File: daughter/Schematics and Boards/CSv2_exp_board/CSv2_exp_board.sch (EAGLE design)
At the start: 144 parts, among them J1 HIROSE-DF40_44-PIN_CONNECTORS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, J2 J-SERIAL-PORT, J3 CORTEX_DEBUG_SMD, J301 HIROSE-DF40_44-PIN_CONNECTORS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, J4 SJ-43514-SMT, J7 J-USB-HIROSE-MICRO-USB, SW1 SPST_TACT-KMR2, SW2 SPST_TACT-KMR2, T1 TPTP10SQ, T10 TPTP10SQ, T11 TPTP10SQ, T2 TPTP10SQ, T3 TPTP10SQ, T4 TPTP10SQ, T5 TPTP10SQ, T6 TPTP10SQ, T7 TPTP10SQ, T8 TPTP10SQ, T9 TPTP10SQ, U1 LOADSWITCH-MIC94164, U10 LOADSWITCH-MIC94164, U11 BMI160, U12 TLV320DAC26IRHB, U13 ADG839YKSZ-500RL7KS_6_ADI-L, U14 LOADSWITCH-MIC94164, U15 LP2980AIM5-2.5/NOPBMF05A_TEX-L, U16 NCP553SQ18T1GSC-82AB_ONS-L, U2 ADA4841-1YRJZ-R7RJ_6-L, U205 MPL3115A2, U3 Value, U4 RFM69HCW, U5 Value, U6 Value, U7 LOADSWITCH-MIC94164, U8 LOADSWITCH-MIC94164, U9 LOADSWITCH-MIC94164, X1 32.768kHz, X2 32.768, X3 uFL, X4 uFL, X5 uFL, X6 uFL

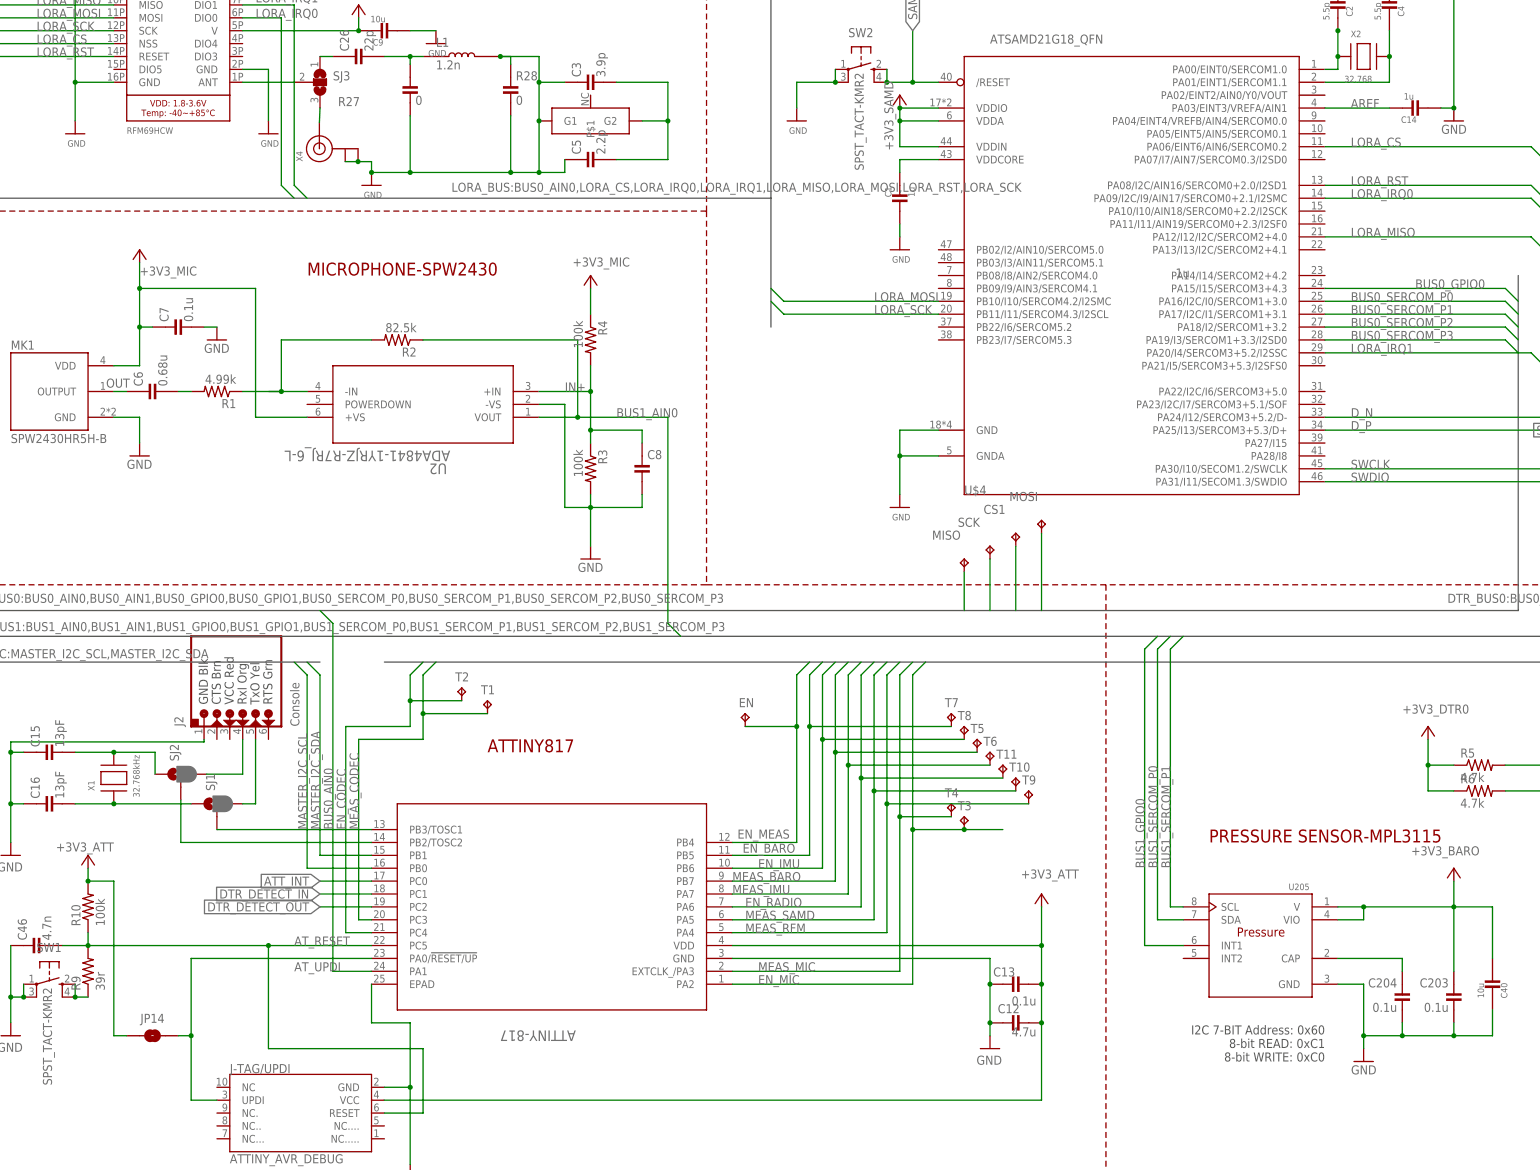
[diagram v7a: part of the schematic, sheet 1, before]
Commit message: DTR-updated BOM
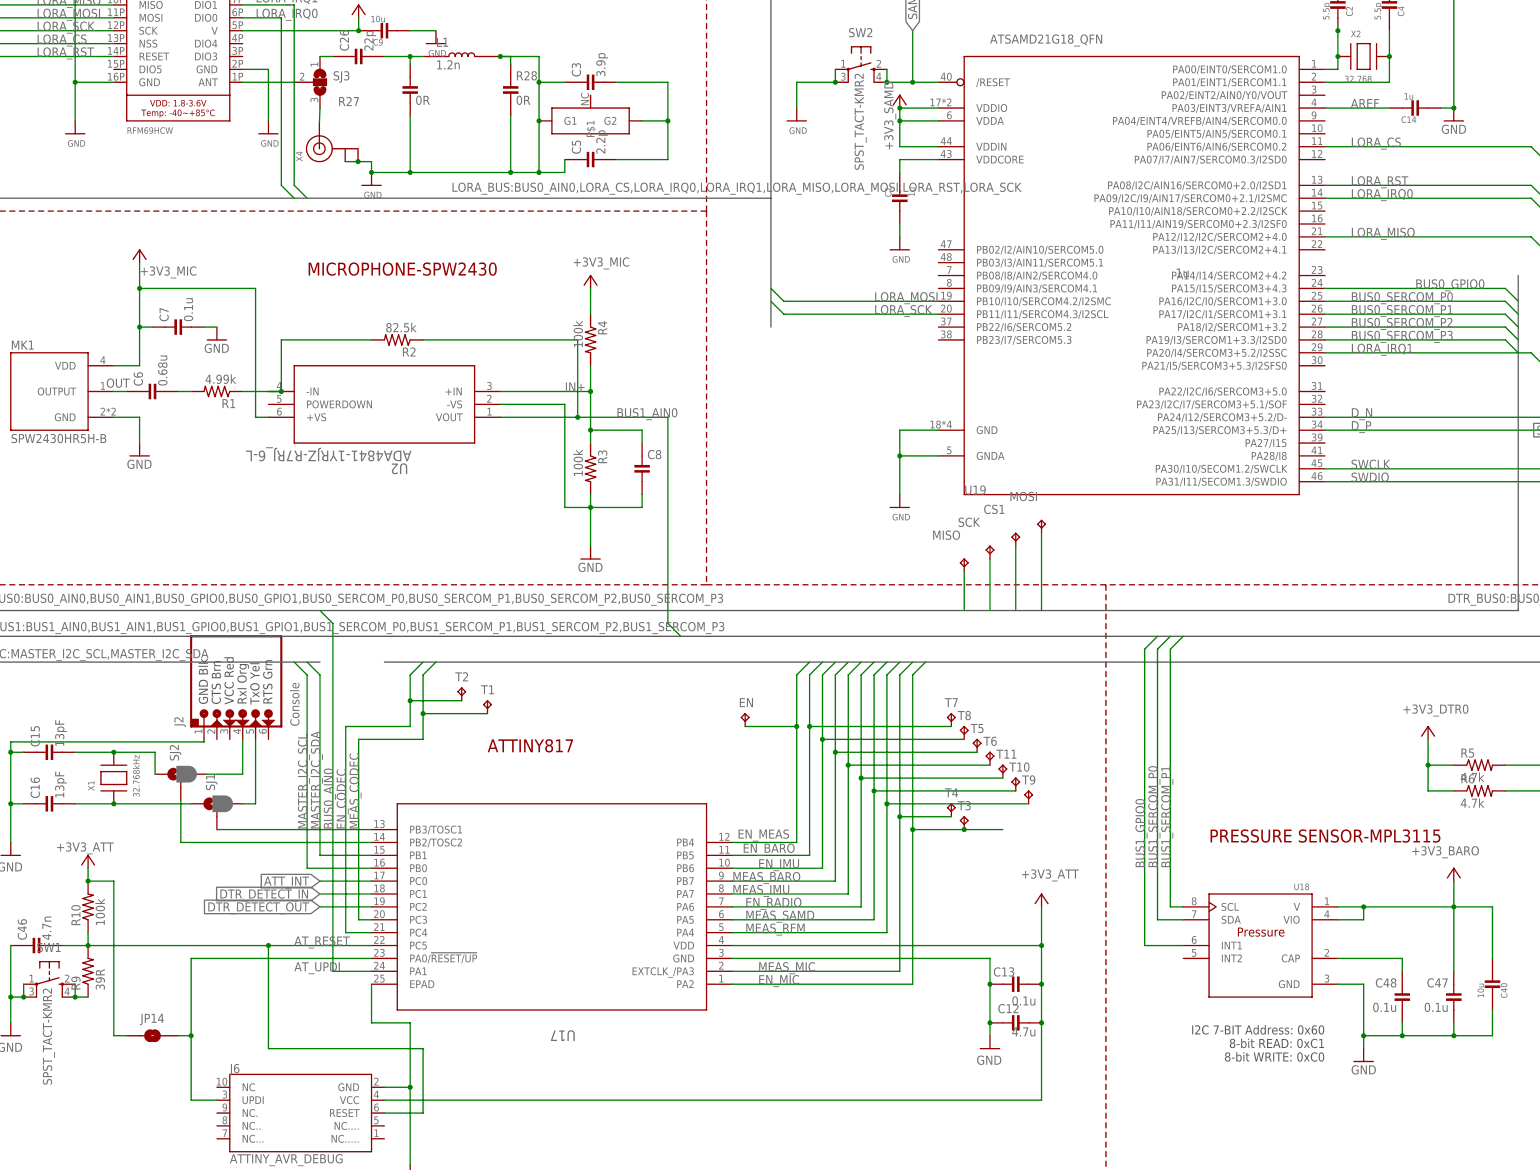
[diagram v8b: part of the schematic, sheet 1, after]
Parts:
- A1: DESC (none) -> RF ANT 915MHZ CHIP SOLDER SMD; MANUFACTURER (none) -> Taoglas; TYPE (none) -> Chip Antenna; Z-HEIGHT (none) -> 0.5mm
- AINT, ASCL, ASDA, CS2, D_IN, D_OUT, JP16, RESET: Z-HEIGHT (none) -> d
- C1, C14: DESC (none) -> CAP CER 1UF 10V X5R 0402; SIZE (none) -> 0402; TYPE (none) -> Capacitor; VOLT (none) -> 10V; Z-HEIGHT (none) -> 0.55mm
- C10, C17, C19, C21, C23, C29: DESC (none) -> CAP CER 1UF 6.3V X5R 0402; HEIGHT (none) -> 0.55mm; SIZE (none) -> 0402; TYPE (none) -> Capacitor; VOLT (none) -> 6.3V
- C11, C18, C20, C22, C30, C43, C44, C45: DESC (none) -> CAP CER 0.1UF 10V X7R 0402; DESCRIPTION (none) -> 0.1µF ±10% 10V Ceramic Capacitor X7R 0402 (1005 Metric); HEIGHT (none) -> 0.55mm; MPN CC0402KRX5R5BB104 -> CC0402KRX7R6BB104; PARTNO CC0402KRX5R5BB104 -> CC0402KRX7R6BB104; SIZE (none) -> 0402; TC X5R -> (none); TYPE (none) -> Capacitor; VOLT (none) -> 10V
- C12: DESC (none) -> CAP CER 4.7UF 10V X5R 0603; HEIGHT (none) -> 0.9mm; SIZE (none) -> 0603; TYPE (none) -> Capacitor; VOLT (none) -> 10V
- C13, C25, C36, C47, C48, C7: DESC (none) -> CAP CER 0.1UF 16V X7R 0402; HEIGHT (none) -> 0.55mm; SIZE (none) -> 0402; TYPE (none) -> Capacitor; VOLT (none) -> 16V
- C15, C16, CS1: TYPE (none) -> Capacitor
- C2: DESC (none) -> CAP CER RF 5.5PF 50V +/-0.1 PF C; SIZE (none) -> 0402; TOL 0.1p -> 0.1pF; TYPE (none) -> Capacitor; VOLT (none) -> 50V; Z-HEIGHT (none) -> 0.55mm
- C24: DESC (none) -> CAP CER 0.1UF 10V X7R 0402; HEIGHT (none) -> 0.55mm; MPN CC0402KRX5R5BB104 -> CC0402KRX7R6BB104; PARTNO CC0402KRX5R5BB104 -> CC0402KRX7R6BB104; SIZE (none) -> 0402; TC X5R -> (none); TYPE (none) -> Capacitor; VOLT (none) -> 10V
- C26: DESC (none) -> CAP CER 22PF 50V C0G/NP0 0402; HEIGHT (none) -> 0.55mm; SIZE (none) -> 0402; TYPE (none) -> Capacitor; VOLT (none) -> 50V
- C3: DESC (none) -> CAP CER 3.9PF 50V C0G/NP0 0402; SIZE (none) -> 0402; TC (none) -> C0G, NP0; TOL 0.05p -> 0.05pF; TYPE (none) -> Capacitor; VOLT (none) -> 50V; Z-HEIGHT (none) -> 0.55mm
- C31, C32: device Capacitors:C-0603 -> Capacitors:C-0805; DESC (none) -> CAP CER 47UF 6.3V X5R 0805; HEIGHT (none) -> 0.95mm; MANUFACTURER AVX -> Murata; MPN 06036D476MAT2A -> GRM219R60J476ME44D; PARTNO 06036D476MAT2A -> GRM219R60J476ME44D; SIZE (none) -> 0805; TYPE (none) -> Capacitor; VOLT (none) -> 6.3V
- C33, C34, C38: DESC (none) -> CAP CER 0.1UF 25V X7R 0402; HEIGHT (none) -> 0.55mm; SIZE (none) -> 0402; TYPE (none) -> Capacitor; VOLT (none) -> 25V
- C35, C39, C40, C9: DESC (none) -> CAP CER 10UF 6.3V X5R 0603; HEIGHT (none) -> 0.9mm; SIZE (none) -> 0603; TYPE (none) -> Capacitor; VOLT (none) -> 6.3V
- C37: DESC (none) -> CAP TANT 10UF 10% 10V 0603; HEIGHT (none) -> 1mm; SIZE (none) -> 0603; TYPE (none) -> Tantalum Capacitor; VOLT (none) -> 10V
- C4: DESC (none) -> CAP CER RF 5.5PF 50V +/-0.1 PF C; SIZE (none) -> 0402; TC C0G,NP0 -> C0G, NP0; TOL 0.1p -> 0.1pF; TYPE (none) -> Capacitor; VOLT (none) -> 50V; Z-HEIGHT (none) -> 0.55mm
- C41: DESC (none) -> CAP TANT 2.2UF 20% 6.3V 0402; HEIGHT (none) -> 0.7mm; MPN (none) -> TACK225M006QTA; SIZE (none) -> 0402; TYPE (none) -> Tantalum Capacitor; VOLT (none) -> 6.3V
- C42: DESC (none) -> CAP CER 1UF 10V X7S 0402; HEIGHT (none) -> 0.55mm; SIZE (none) -> 0402; TYPE (none) -> Capacitor; VOLT (none) -> 10V
- C46: DESC (none) -> CAP CER 4700PF 25V X7R 0402; HEIGHT (none) -> 0.55mm; SIZE (none) -> 0402; TYPE (none) -> Capacitor; VOLT (none) -> 25
- C5: DESC (none) -> CAP CER 2.2PF 50V C0G/NP0 0402; HEIGHT (none) -> 0.55mm; SIZE (none) -> 0402; TC (none) -> C0G, NP0; TOL 0.05p -> 0.05pF; TYPE (none) -> Capacitor; VOLT (none) -> 50V
- C6: DESC (none) -> CAP CER 0.68UF 6.3V X5R 0402; HEIGHT (none) -> 0.55mm; SIZE (none) -> 0402; TYPE (none) -> Capacitor; VOLT (none) -> 6.3V
- C8: DESC (none) -> CAP CER 1UF 10V X5R 0402; SIZE (none) -> 0402; TOL (none) -> 20%; TYPE (none) -> Capacitor; VOLT (none) -> 10V; Z-HEIGHT (none) -> 0.55mm
- J1: DESC (none) -> CONN RCPT 44POS SMD GOLD; HEIGHT (none) -> 3mm; MANUFACTURER (none) -> Hirose; TYPE (none) -> Receptor
- J2: DESC (none) -> CONN HEADER VERT 6POS 2.54MM; TYPE (none) -> Header
- J3, J6: DESC (none) -> CONN HEADER SMD 10POS 1.27MM; MANUFACTURER (none) -> Samtec; TYPE (none) -> Header
- J4: DESC (none) -> CONN JACK 4COND 3.5MM SMD R/A; HEIGHT (none) -> 5mm; MANUFACTURER (none) -> CUI Devices; TYPE (none) -> Audio Jack
- J5: DESC (none) -> CONN PLUG 44POS SMD GOLD; MANUFACTURER (none) -> Hirose; TYPE (none) -> Header
- J7: DESC (none) -> CONN RCPT USB2.0 MICRO AB SMD RA; TYPE (none) -> Receptor
- L1: DESC (none) -> FIXED IND 1.2NH 390MA 100 MOHM; HEIGHT (none) -> 0.45mm; MANUFACTURER (none) -> Murata; SIZE (none) -> 0402; TOL (none) -> 0.05nH; TYPE (none) -> Inductor
- MK1: DESC (none) -> MAMET MIC ANALOG TOP PORT; HEIGHT (none) -> 1.1mm; MANUFACTURER (none) -> Knowles; SIZE (none) -> 0.122" L x 0.098" W (3.10mm x 2.50mm); TYPE (none) -> MEMS Microphone; VOLT (none) -> 1.5V ~ 3.6V
- R1: DESC (none) -> RES SMD 4.99KOHM 0.1% 1/16W 0402; HEIGHT (none) -> 0.4mm; SIZE (none) -> 0402; TC (none) -> ±25ppm/°C; TYPE (none) -> Resistor
- R10, R11: DESC (none) -> RES SMD 100K OHM 1% 1/10W 0402; HEIGHT (none) -> 0.4mm; SIZE (none) -> 0402; TC (none) -> ±100ppm/°C; TYPE (none) -> Resistor
- R12: value (none) -> 0R; DESC (none) -> RES SMD 0 OHM JUMPER 1/2W 1210; HEIGHT (none) -> 0.7mm; MPN (none) -> ERJ-14Y0R00U; SIZE (none) -> 1210; TYPE (none) -> Resistor
- R2: DESC (none) -> RES SMD 82.5KOHM 0.1% 1/16W 0402; HEIGHT (none) -> 0.4mm; SIZE (none) -> 0402; TC (none) -> ±25ppm/°C; TYPE (none) -> Resistor
- R27, R28: value 0 -> 0R; DESC (none) -> RES 0 OHM JUMPER 1/16W 0402; SIZE (none) -> 0402; TYPE (none) -> Resistor
- R3, R4: DESC (none) -> RES SMD 100K OHM 0.1% 1/16W 0402; HEIGHT (none) -> 0.35mm; SIZE (none) -> 0402; TC (none) -> ±25ppm/°C; TYPE (none) -> Resistor
- R5, R6: DESC (none) -> RES SMD 4.7K OHM 1% 1/10W 0402; HEIGHT (none) -> 0.4mm; SIZE (none) -> 0402; TC (none) -> ±100ppm/°C; TYPE (none) -> Resistor
- R7: value 50 -> 50R; device Resistors:R-0805 -> Resistors:R-0402; DESC (none) -> RES SMD 50 OHM 0.1% 1/20W 0402; HEIGHT (none) -> 0.84mm; MPN (none) -> FC0402E50R0BST1; PARTNO Y402250R0000A9R -> FC0402E50R0BST1; SIZE (none) -> 0402; TC (none) -> ±25ppm/°C; TOL 0.05% -> 0.1%; TYPE (none) -> Resistor
- R8: DESC (none) -> RES SMD 2.2K OHM 5% 1/10W 0603; HEIGHT (none) -> 0.55mm; SIZE (none) -> 0603; TC (none) -> ±200ppm/°C; TYPE (none) -> Resistor
- R9: value 39r -> 39R; DESC (none) -> RES SMD 39 OHM 1% 1/10W 0402; HEIGHT (none) -> 0.4mm; SIZE (none) -> 0402; TC (none) -> ±100ppm/°C; TYPE (none) -> Resistor
- R_SENSE: value 1.33 -> 1.33R; DESC (none) -> RES SMD 1.33 OHM 1% 1/16W 0402; HEIGHT (none) -> 0.4mm; SIZE (none) -> 0402; TC (none) -> ±100ppm/°C; TYPE (none) -> Resistor
- SW1, SW2: DESC (none) -> SWITCH TACTILE SPST-NO 0.05A 32V; HEIGHT (none) -> 1.9mm; MANUFACTURER (none) -> C&K; SIZE (none) -> 4.60mm x 2.80mm; TYPE (none) -> Switch
- U1, U10, U14, U7, U8, U9: DESC (none) -> IC PWR SWITCH P-CHAN 1:1 6WLCSP; HEIGHT (none) -> 0.65mm; SIZE (none) -> 6-WLCSP (1x1.5); TYPE (none) -> Power Switch
- U11: DESC (none) -> IMU ACCEL/GYRO I2C/SPI 14LGA; HEIGHT (none) -> 0.83mm; MANUFACTURER (none) -> Bosch; SIZE (none) -> 14-LGA (2.5x3); TYPE (none) -> IMU
- U12: DESC (none) -> IC DAC 24BIT 96K 32VQFN; HEIGHT (none) -> 0.9mm; MPN (none) -> TLV320DAC26IRHB; SIZE (none) -> 32-VQFN (5x5); TYPE (none) -> Codec
- U13: DESC (none) -> IC SWITCH SPDT SC70-6; HEIGHT (none) -> 0.9mm; SIZE (none) -> SC-70-6; TYPE (none) -> SPDT Switch
- U15: DESC (none) -> IC REG LINEAR 3V 50MA SOT23-5; HEIGHT (none) -> 0.9-1.45mm; MANUFACTURER (none) -> Texas Instruments; MPN (none) -> LP2980AIM5-3.0/NOPB; SIZE (none) -> SOT-23-5; TYPE (none) -> LDO
- U16: DESC (none) -> IC REG LINEAR 1.8V 80MA SC82AB; HEIGHT (none) -> 0.8-1.1mm; MANUFACTURER (none) -> ON Semiconductor; SIZE (none) -> SC-82AB; TYPE (none) -> LDO
- U17: DESC (none) -> IC MCU 8BIT 8KB FLASH 24QFN; HEIGHT (none) -> 0.85mm; MANUFACTURER (none) -> Microchip; MPN (none) -> ATTINY817MFR; SIZE (none) -> 24-QFN (4x4); TYPE (none) -> MCU
- U18: DESC (none) -> IC ALTIMETER I2C VERSION 8LGA; HEIGHT (none) -> 1.1mm; SIZE (none) -> 8-LGA; TYPE (none) -> Altimeter
- U19: DESC (none) -> IC MCU 32BIT 256KB FLASH 48QFN; HEIGHT (none) -> 0.85mm; MANUFACTURER (none) -> Microchip; MPN ATSAMD21G18A-MFT -> ATSAMD21G18A-MF; PARTNO ATSAMD21G18A-MFT -> ATSAMD21G18A-MF; SIZE (none) -> 48-QFN (7x7); TYPE (none) -> MCU
- U2: DESC (none) -> IC OPAMP VFB 1 CIRCUIT SOT23-6; HEIGHT (none) -> 0.95-1.45mm; MANUFACTURER (none) -> Analog Devices; SIZE (none) -> SOT-23-6; SPICEPREFIX X -> (none); TYPE (none) -> Opamp
- U3, U5, U6: DESC (none) -> IC SWITCH SPDT DUAL 10VSSOP; HEIGHT (none) -> 1.1mm; SIZE (none) -> 10-VSSOP; TYPE (none) -> SPDT Switch
- U4: DESC (none) -> RX TXRX MODULE ISM < 1GHZ SMD; TYPE (none) -> Radio
- X2: TOL 20ppm -> (none)
- X3, X5, X6: HEIGHT (none) -> d
- renumbered ATTINY-817 to U17, C203 to C47, C204 to C48, J-TAG/UPDI to J6, J301 to J5, U$4 to U19, U205 to U18
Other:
- moved on the sheet: U2
